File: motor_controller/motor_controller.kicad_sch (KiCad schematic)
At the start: 99 parts, among them J1 etm, J2 Conn_01x06_MountingPin, J3 Conn_01x06_MountingPin, J4 Conn_01x03, U2 INA186A3IYFDR, U3 STM32G474VEHx

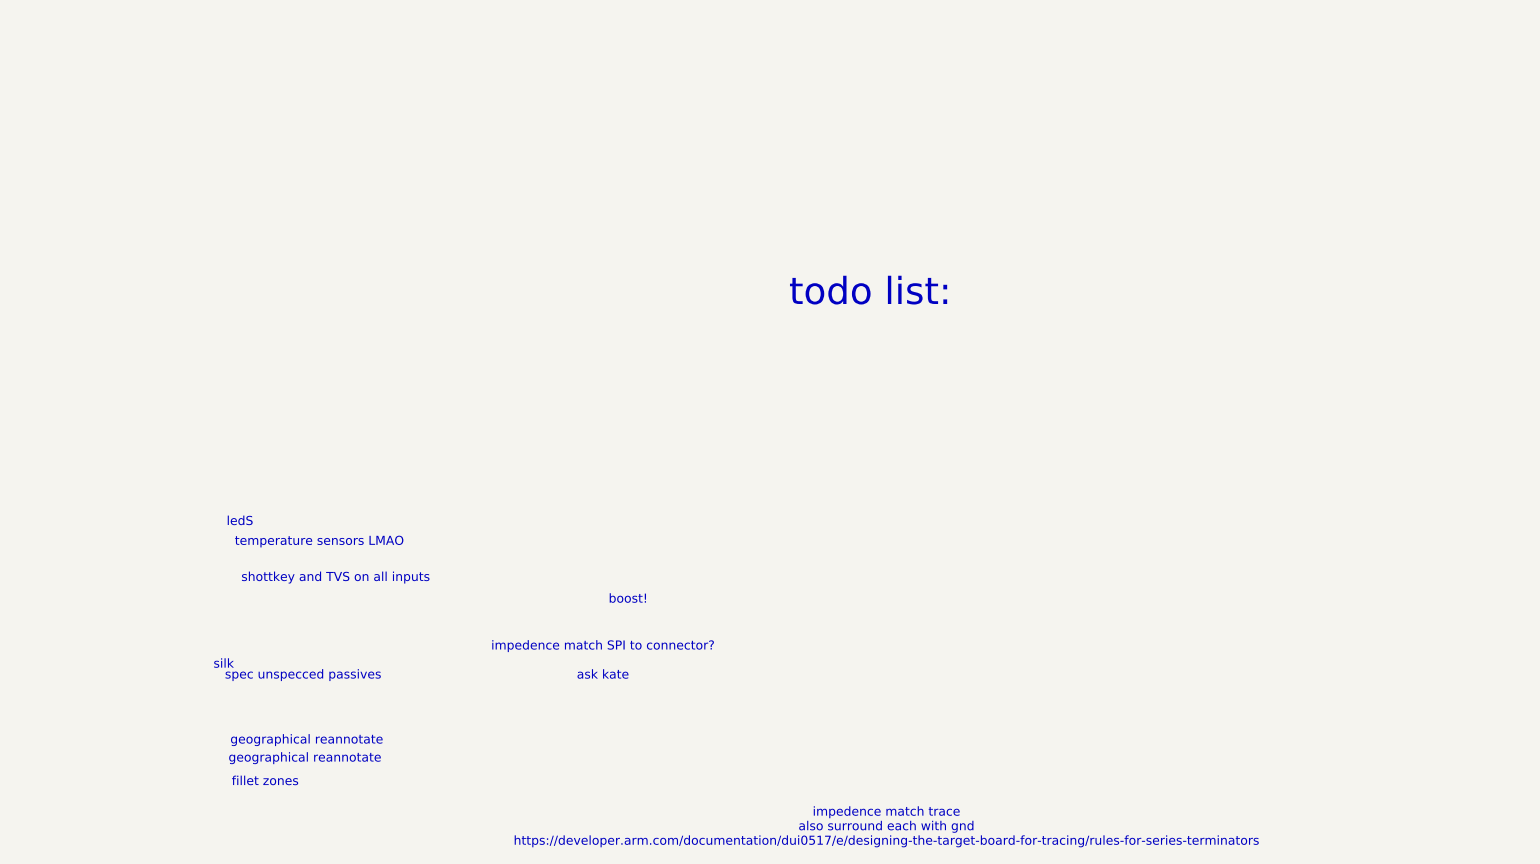
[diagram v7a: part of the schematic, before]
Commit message: didn't save schematic
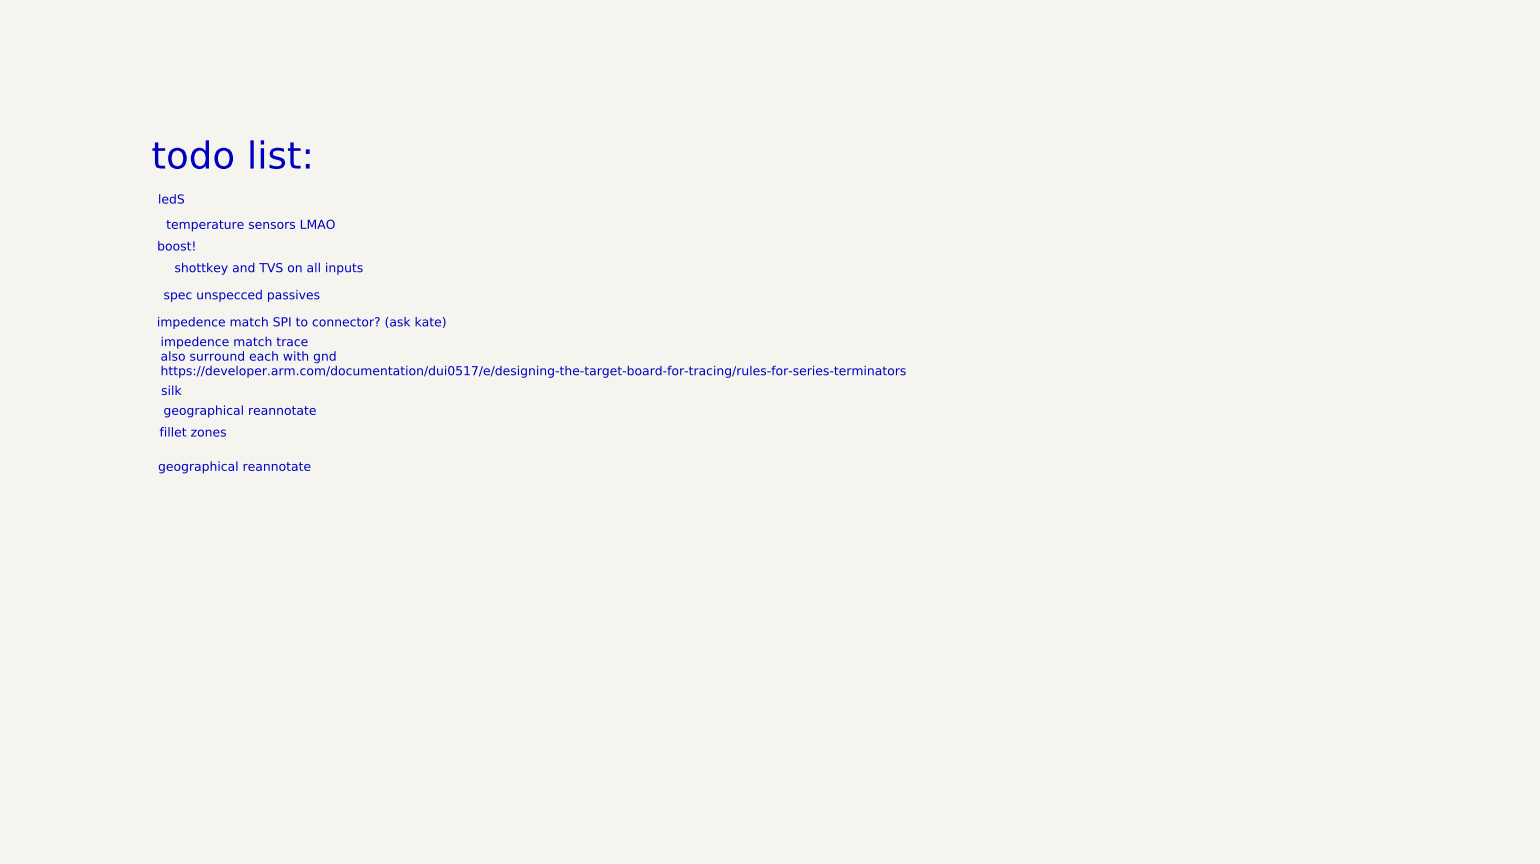
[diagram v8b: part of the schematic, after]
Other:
- note added: "impedence match SPI to connector? (ask kate)"
- note removed: "impedence match SPI to connector? ask kate"
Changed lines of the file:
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@@
 		)
 	)
-	(text "impedence match SPI to connector?\n\nask kate"
-		(exclude_from_sim no)
-		(at 97.79 283.464 0)
-		(effects
-			(font
-				(size 1.27 1.27)
-			)
+	(text "impedence match SPI to connector? (ask kate)"
+		(exclude_from_sim no)
+		(at 35.052 235.966 0)
+		(effects
+			(font
+				(size 1.27 1.27)
+			)
+			(justify left)
 		)
 	)
@@
 	(text "geographical reannotate"
 		(exclude_from_sim no)
-		(at 55.88 297.18 0)
+		(at 45.974 256.286 0)
 		(effects
 			(font
@@
 	(text "temperature sensors LMAO"
 		(exclude_from_sim no)
-		(at 57.912 266.7 0)
+		(at 48.26 222.25 0)
 		(effects
 			(font
@@
 	(text "boost!"
 		(exclude_from_sim no)
-		(at 101.346 274.828 0)
+		(at 37.846 225.298 0)
 		(effects
 			(font
@@
 	(text "impedence match trace\nalso surround each with gnd\nhttps://developer.arm.com/documentation/dui0517/e/designing-the-target-board-for-tracing/rules-for-series-terminators"
 		(exclude_from_sim no)
-		(at 137.668 306.832 0)
-		(effects
-			(font
-				(size 1.27 1.27)
-			)
+		(at 35.56 240.792 0)
+		(effects
+			(font
+				(size 1.27 1.27)
+			)
+			(justify left)
 		)
 	)
@@
 	(text "silk"
 		(exclude_from_sim no)
-		(at 44.45 283.972 0)
+		(at 37.084 245.618 0)
 		(effects
 			(font
@@
 	(text "spec unspecced passives"
 		(exclude_from_sim no)
-		(at 55.626 285.496 0)
+		(at 46.99 232.156 0)
 		(effects
 			(font
@@
 	(text "ledS\n"
 		(exclude_from_sim no)
-		(at 46.736 263.906 0)
+		(at 37.084 218.694 0)
 		(effects
 			(font
@@
 	(text "shottkey and TVS on all inputs"
 		(exclude_from_sim no)
-		(at 60.198 271.78 0)
+		(at 50.8 228.346 0)
 		(effects
 			(font
@@
 	(text "fillet zones\n"
 		(exclude_from_sim no)
-		(at 50.292 300.482 0)
+		(at 40.132 251.46 0)
 		(effects
 			(font
@@
 	(text "todo list:\n"
 		(exclude_from_sim no)
-		(at 135.382 231.648 0)
+		(at 45.72 212.598 0)
 		(effects
 			(font
@@
 	(text "geographical reannotate"
 		(exclude_from_sim no)
-		(at 56.134 294.64 0)
-		(effects
-			(font
+		(at 46.736 248.412 0)
+		(effects
+			(font
